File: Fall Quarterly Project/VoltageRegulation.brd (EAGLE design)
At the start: 160 x 100 mm, 19 parts

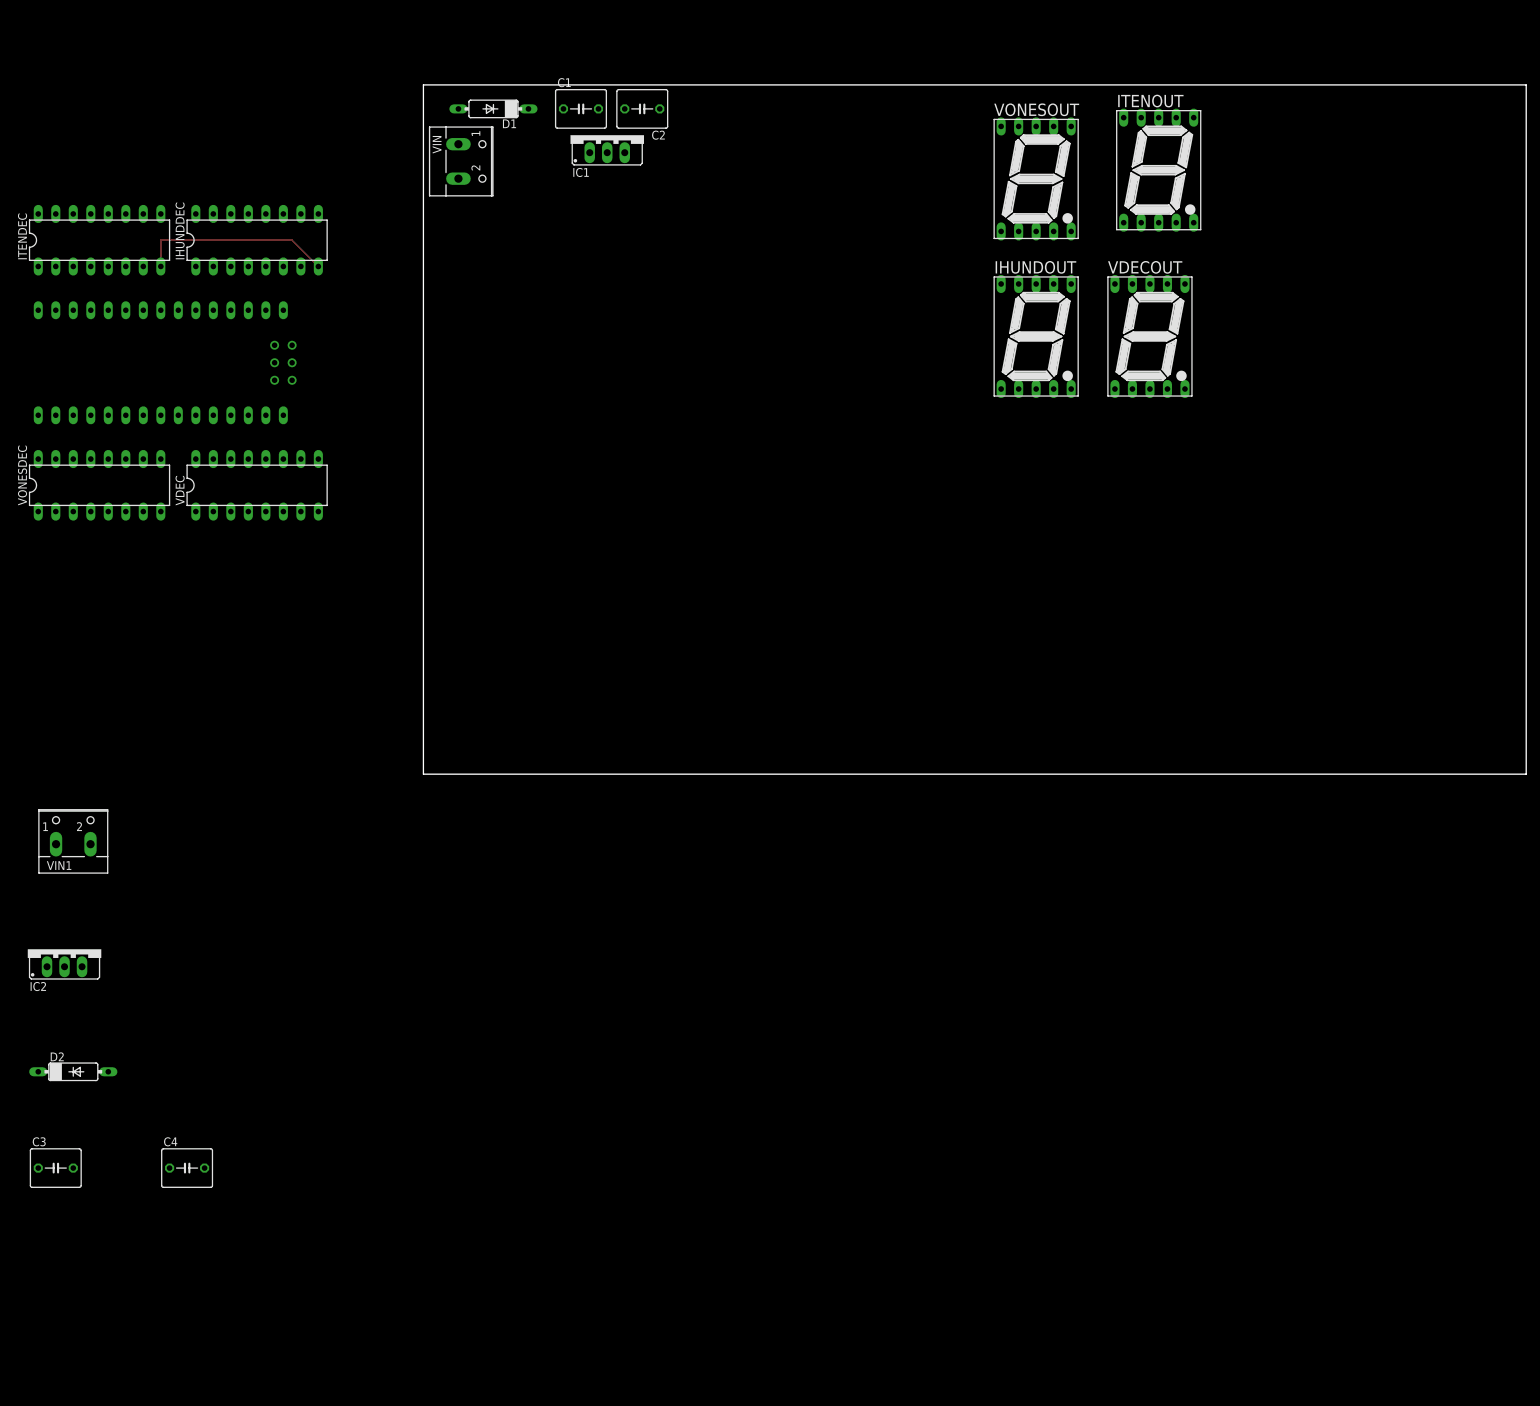
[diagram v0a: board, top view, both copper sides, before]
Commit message: Update 1.2
Introduced part of the voltage sense circuitry, filter, and amplifier. most parts still need values though, those of you with r or c values can feel free to label them.
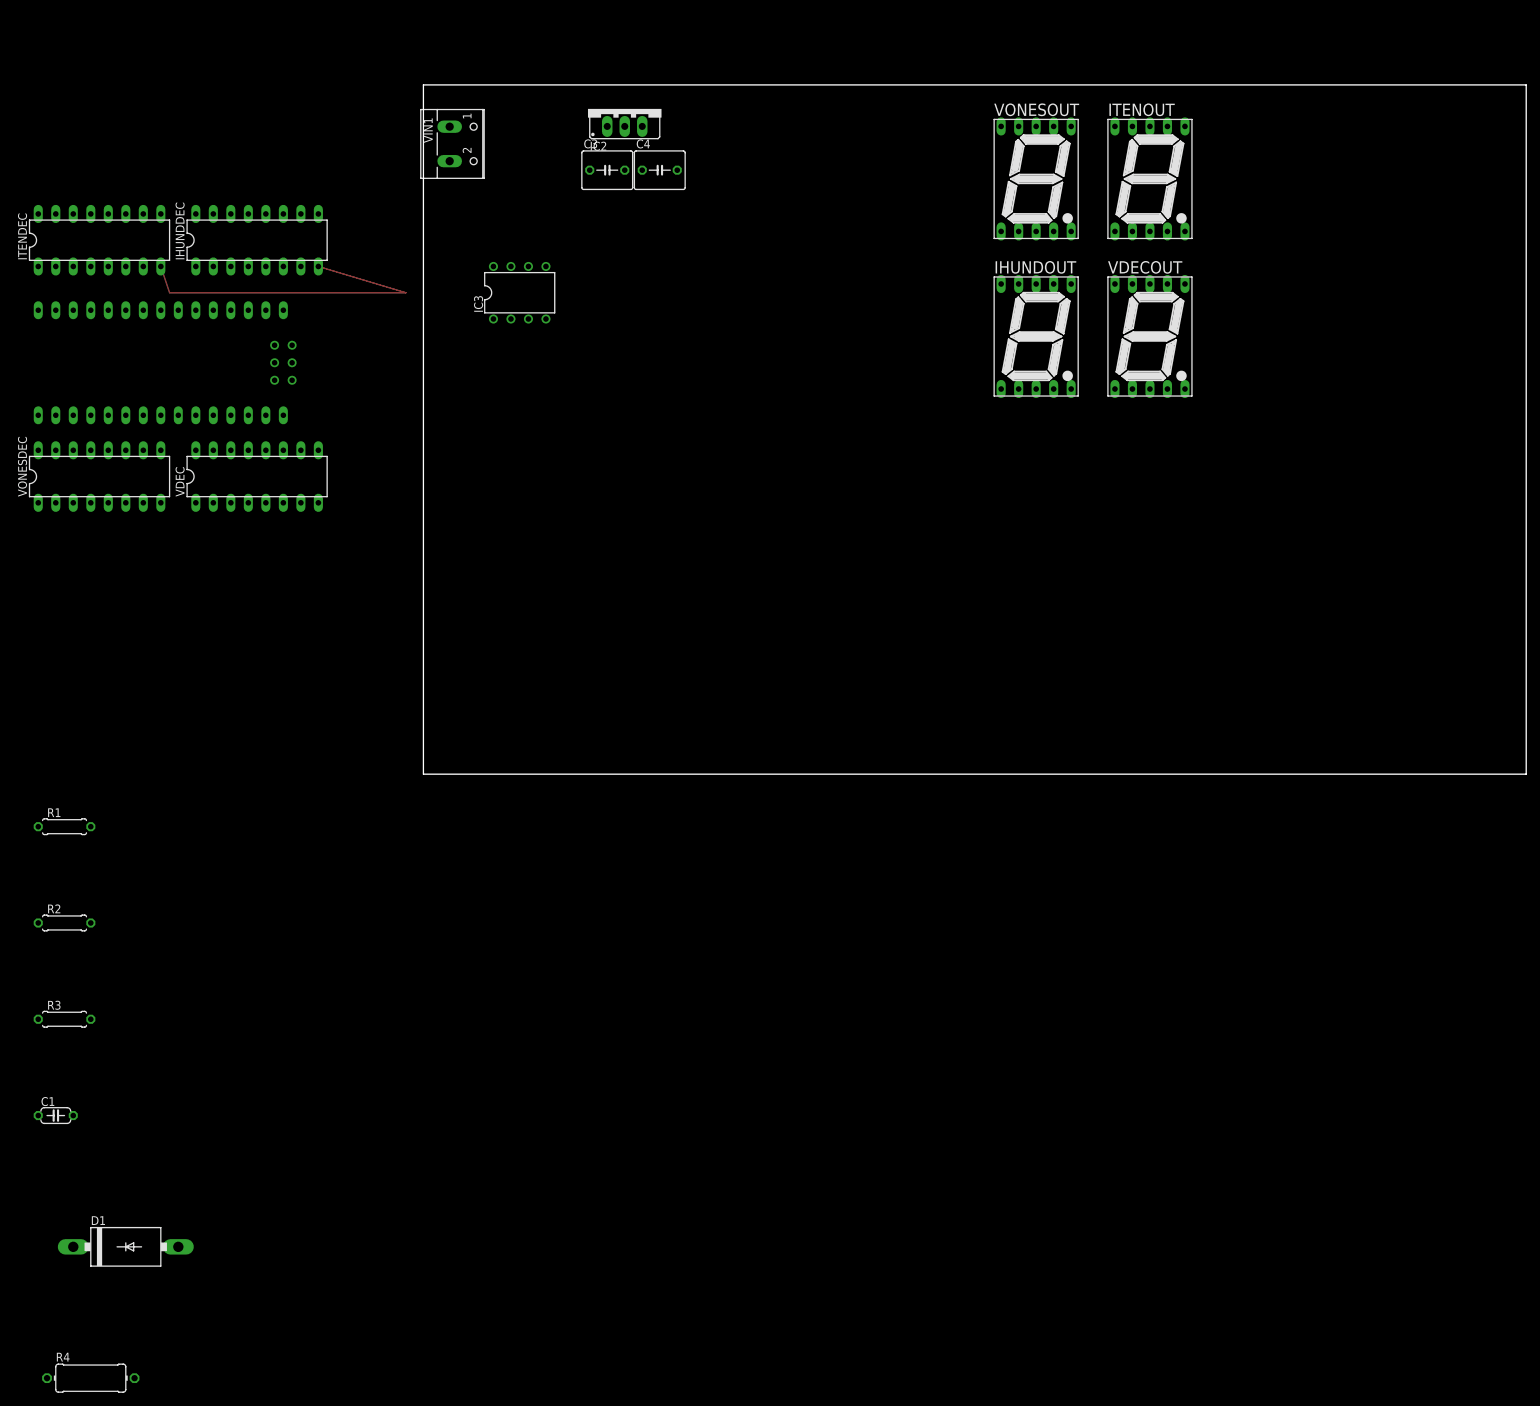
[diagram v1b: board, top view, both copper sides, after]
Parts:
- removed C2: (no value), rcl:C050-055X075
- removed D2: (no value), diode:DO07
- removed IC1: (no value), v-reg:78XXS
- removed VIN: (no value), con-wago-500:W237-102
- added IC3: L272M, linear:DIL08
- added R1: 30k, rcl:0207/7
- added R2, R3: 10k, rcl:0207/7
- added R4: (no value), rcl:0411/12
- C1: device rcl:C050-055X075 -> rcl:C050-024X044
- D1: value (none) -> SB320; device diode:DO07 -> diode:DO201-15
- moved D1 173.5 mm to (-43.2, -68.6), turned to 0 degrees
- moved C3 165.4 mm to (26.7, 87.6)
- moved C1 164.7 mm to (-53.3, -49.5)
- moved C4 160.2 mm to (34.3, 87.6)
- moved IC2 146.5 mm to (29.2, 96.5)
- moved VIN1 114.8 mm to (5.08, 91.4), turned to 270 degrees
- moved ITENOUT 1.80 mm to (105.4, 86.4)
- moved VDEC 1.27 mm to (-24.1, 43.2)
- moved VONESDEC 1.27 mm to (-47.0, 43.2)
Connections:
- new net N$2: IC3.1, IC3.6, R1.2, R4.1
- new net N$4: IC3.8, R1.1, R2.1
- new net N$5: C1.1, IC3.7, R3.2
- new net N$6: IC3.5, R4.2
- net +12V: now also IC3.2; no longer C1.1, D2.C, IC1.IN
- net +5V: no longer C2.1, IC1.OUT
- net 10SDIGIT5: now also U$1.D12; no longer U$1.D11
- net GND: now also IC3.4, R2.2; no longer C2.2, IC1.GND, VIN.2
- net N$1: now also R3.1, U$1.D11; no longer D1.A, VIN.1
- net N$3: now also D1.A; no longer D2.A
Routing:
- net VSS: track 28.2 -> 51.6 mm

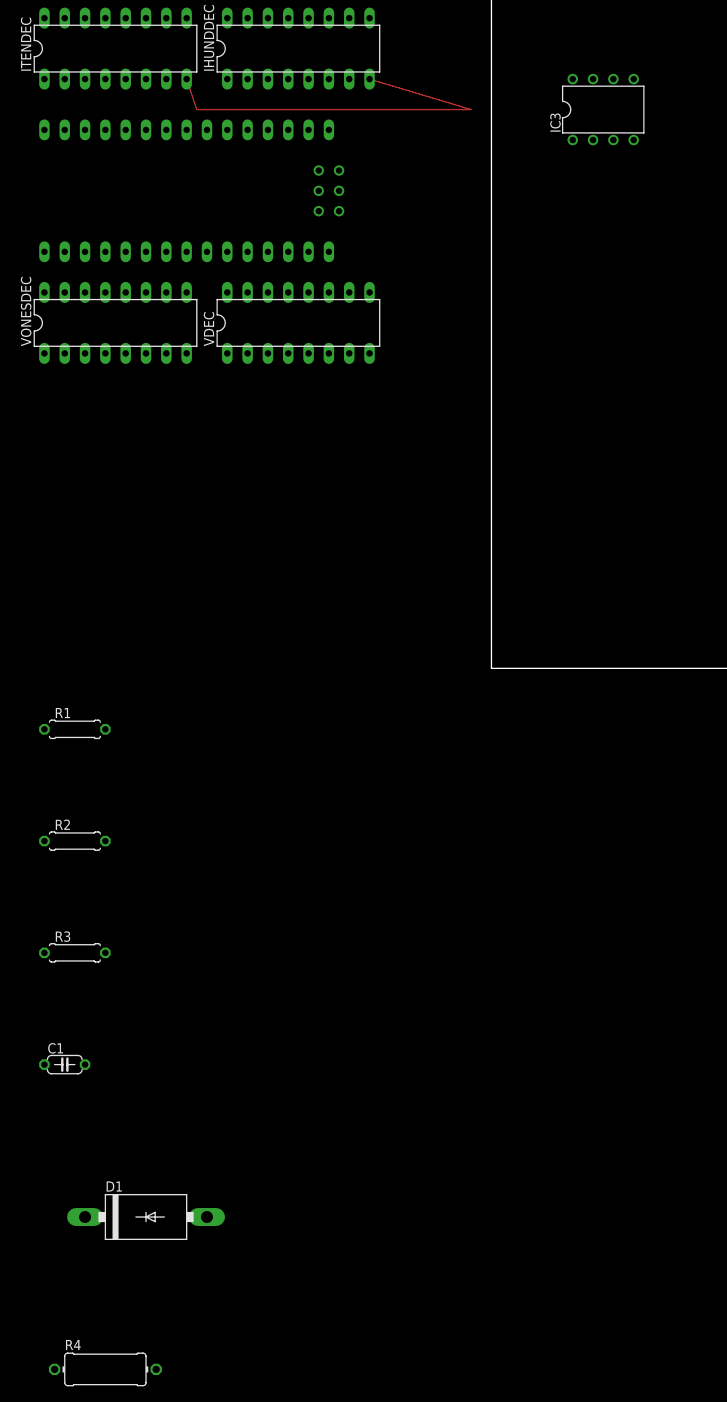
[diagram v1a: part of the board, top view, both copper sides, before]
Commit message: Update 1.3
All major parts have now been included in the schematic, only adjustments need to be made now. I know some resistor values have been implemented with series or parallel combinations in order use stockroom parts, and this is not accounted for. Values still need to be added to parts for the bill of materials as well as the silkscreening process. I've tried laying some traces as well in the board layout, but the config i've been trying out seems bad and needs an entire rework. We are at the point that board layout and tracing can commence.
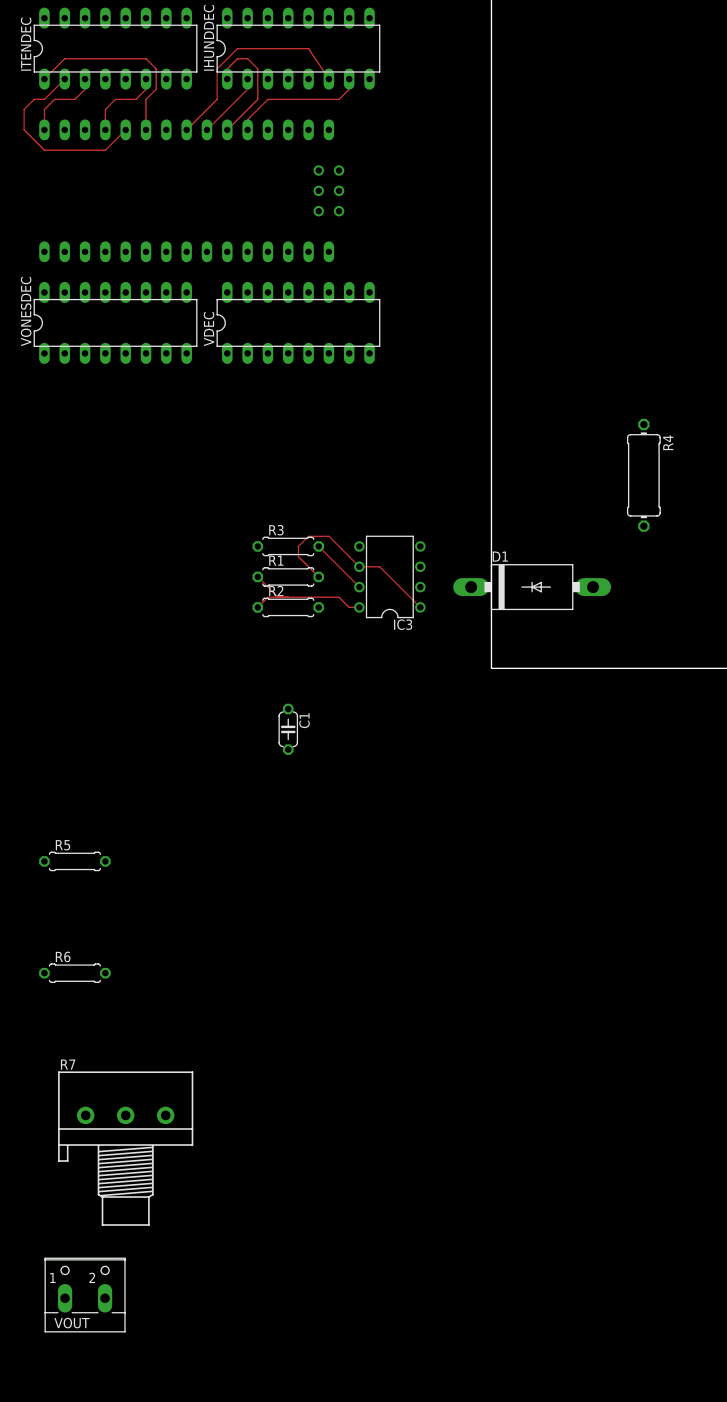
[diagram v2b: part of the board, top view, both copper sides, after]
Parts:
- added R5, R6: 30k, rcl:0207/7
- added R7: (no value), pot:3RP/1610N
- added VOUT: (no value), con-wago-500:W237-102
- moved R4 130.5 mm to (19.1, 24.1), turned to 270 degrees
- moved D1 92.4 mm to (5.08, 10.2)
- moved IC3 64.2 mm to (-12.7, 11.4), turned to 90 degrees
- moved R3 57.4 mm to (-25.4, 15.2)
- moved C1 50.4 mm to (-25.4, -7.62), turned to 270 degrees
- moved R2 39.6 mm to (-25.4, 7.62)
- moved R1 32.8 mm to (-25.4, 11.4)
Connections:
- new net N$10: IC3.3, U$1.A2
- new net N$7: R5.1, R6.2, U$1.A1
- new net N$9: R7.2, U$1.A0
- net +5V: now also R7.3
- net GND: now also R6.1, R7.1, VOUT.1
- net N$6: now also R5.2, VOUT.2
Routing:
- net VSS: track 51.6 -> 0.00 mm
- net 10SDIGIT4: track 0.00 -> 26.3 mm
- net 1SDIGIT3: track 0.00 -> 25.3 mm
- net N$2: track 0.00 -> 24.3 mm
- net 1SDIGIT2: track 0.00 -> 23.7 mm
- net N$4: track 0.00 -> 18.6 mm
- net 10SDIGIT1: track 0.00 -> 16.8 mm
- net 10SDIGIT2: track 0.00 -> 16.0 mm
- net 10SDIGIT5: track 0.00 -> 9.94 mm
- net 1SDIGIT4: track 0.00 -> 9.94 mm
- net 10SDIGIT3: track 0.00 -> 8.45 mm
- net N$5: track 0.00 -> 7.18 mm
